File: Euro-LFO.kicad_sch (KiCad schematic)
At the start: 32 parts, among them J1 Conn_02x05_Odd_Even, Q1 NPN, U1 TL074

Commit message: updated
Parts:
- removed Q1: NPN, Package_TO_SOT_SMD:SOT-23, symbol Simulation_SPICE:NPN
- added D4, D5: SS14 (40 V 1 A Schottky), Diode_SMD:D_SMA, symbol Device:D_Schottky
- added J2: Conn_02x10_Odd_Even, symbol Connector_Generic:Conn_02x10_Odd_Even
- added Q1: MMBT3904, Package_TO_SOT_SMD:SOT-23, symbol Transistor_BJT:MMBT3904
- added R23, R24: 10 Ω 0805, Resistor_SMD:R_0805_2012Metric, symbol Device:R_US
- C1, C2: value 47n -> 100 nF 50 V X7R; LCSC (none) -> C49678
- C3: value 47n -> 00 nF 50 V X7R; LCSC (none) -> C49678
- C6, C7: value 47µ -> 10 µF 25 V X5R; footprint (none) -> Capacitor_SMD:C_0805_2012Metric; symbol Device:C_Polarized_Small_US -> Device:C; LCSC (none) -> C15850
- D1, D2: value 1N914 -> 1N4148W; LCSC (none) -> C81598
- D3: value LED -> 3 mm LED
- INV-OUT1, PWM-OUT1, TRI-OUT1: value (none) -> 3.5 mm mono jack, Thonkiconn PJ398SM
- J1: value Conn_02x05_Odd_Even -> 2×5 2.54 mm shrouded IDC box header; footprint Connector_PinHeader_2.54mm:PinHeader_2x05_P2.54mm_Vertical -> Connector_IDC:IDC-Header_2x05_P2.54mm_Vertical
- OFFSET1: value 100K -> 100 kΩ B (linear), centre-detent if available
- R1: value 150K -> 150 kΩ 0805 1%; LCSC (none) -> C17557
- R14, R4: value 4K7 -> 4.7 kΩ 0805 1%; LCSC (none) -> C17673
- R16: value 100K -> 100 kΩ 0805 1%
- R17, R20: value 1K -> 1 kΩ 0805 1%; LCSC (none) -> C17513
- R18, R19, R21, R22, R5: value 100K -> 100 kΩ 0805 1%; LCSC (none) -> C149504
- R2: value 2K2 -> 2.2 kΩ 0805 1%; LCSC (none) -> C17726
- R3: value 1K -> 1 kΩ 0805; LCSC (none) -> C17513
- R6: value 10K -> 10 kΩ 0805 1%; LCSC (none) -> C17414
- RANGE1: value 100K -> 100 kΩ A (audio) for smoother level control (B works)
- RATE1: value 100K -> 100 kΩ Alpha 9 mm vertical - taper B (or reverse‑log for feel)
- SHAPE1: value 500K -> 500 kΩ B (linear)
- U1: value TL074 -> TL074CDR; LCSC (none) -> C6961
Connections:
- net +12V: now also Q1.3 (C), R23.1; no longer J1.1 (Pin_1), J1.2 (Pin_2)
- net -12V: now also R24.1; no longer J1.10 (Pin_10), J1.9 (Pin_9)
- net GND: now also J2.19 (Pin_19)
- net at R14.1: now also Q1.2 (E)
- net LED_A: now reaches D3.2 (A), R14.2
- net LED_A: now also J2.1 (Pin_1)
- net INV-OUT-A: now reaches INV-OUT1.T, R20.1
- net INV-OUT-A: now also J2.3 (Pin_3)
- net at C1.2, R5.1, RANGE1.1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: now also Q1.1 (B)
- net TRI-OUT-A: now reaches R17.1, TRI-OUT1.T
- net TRI-OUT-A: now also J2.5 (Pin_5)
- new net: D5.1 (K), J1.1 (Pin_1), J1.2 (Pin_2)
- new net: D5.2 (A), R24.2
- new net: D4.2 (A), J1.10 (Pin_10), J1.9 (Pin_9)
- new net: D4.1 (K), R23.2
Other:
- moved on the sheet: C2, C3, D2, D3, INV-OUT1, J1, TRI-OUT1, U1E

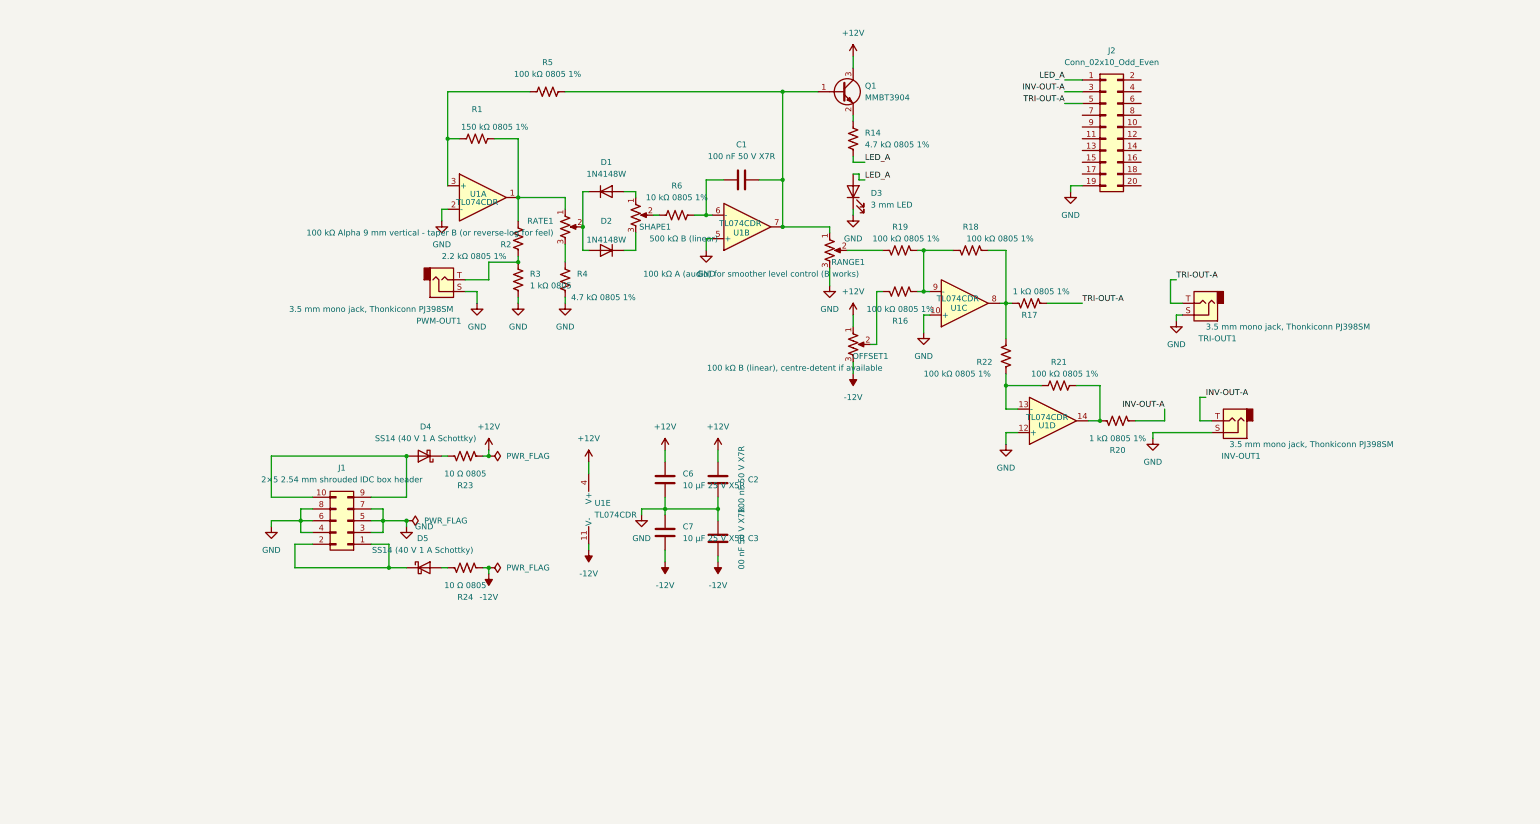
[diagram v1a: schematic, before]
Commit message: added pin headers
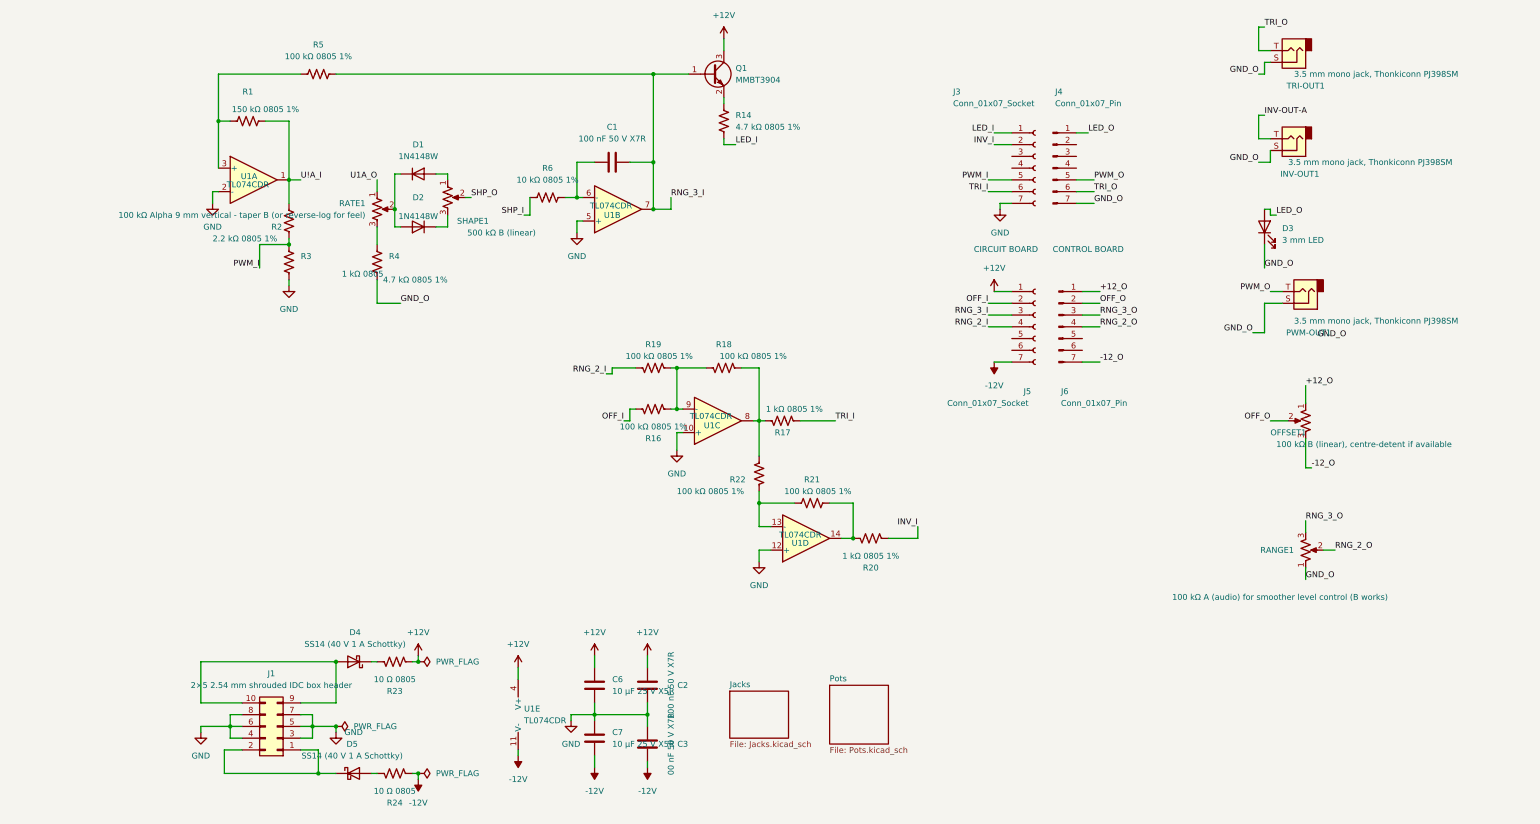
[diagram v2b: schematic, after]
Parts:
- removed J2: Conn_02x10_Odd_Even, symbol Connector_Generic:Conn_02x10_Odd_Even
- added J3, J5: Conn_01x07_Socket, Connector_PinHeader_2.54mm:PinHeader_1x07_P2.54mm_Vertical, symbol Connector:Conn_01x07_Socket
- added J4, J6: Conn_01x07_Pin, Connector_PinHeader_2.54mm:PinHeader_1x07_P2.54mm_Vertical, symbol Connector:Conn_01x07_Pin
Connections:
- net +12V: now also J5.1 (Pin_1); no longer OFFSET1.1
- net -12V: now also J5.7 (Pin_7); no longer OFFSET1.3
- net GND: now also J3.7 (Pin_7); no longer D3.1 (K), INV-OUT1.S, PWM-OUT1.S, R4.1, RANGE1.3, TRI-OUT1.S
- net INV-OUT-A: no longer R20.1
- net U!A_I: now reaches R1.2, R2.2, U1.1
- net U!A_I: no longer RATE1.1
- net PWM_I: now reaches R2.1, R3.2
- net PWM_I: now also J3.5 (Pin_5); no longer PWM-OUT1.T
- net OFF_I: now reaches R16.2
- net OFF_I: now also J5.2 (Pin_2); no longer OFFSET1.2
- net RNG_3_I: now reaches C1.2, Q1.1 (B), R5.1, U1.7
- net RNG_3_I: now also J5.3 (Pin_3); no longer RANGE1.1
- net SHP_I: now reaches R6.2
- net SHP_I: no longer SHAPE1.2
- net RNG_2_I: now reaches R19.2
- net RNG_2_I: now also J5.4 (Pin_4); no longer RANGE1.2
- net LED_A renamed LED_I
- net LED_I: now also J3.1 (Pin_1); no longer D3.2 (A)
- net TRI-OUT-A renamed TRI_I
- net TRI_I: now also J3.6 (Pin_6); no longer TRI-OUT1.T
- new net +12_O: J6.1 (Pin_1), OFFSET1.1
- new net -12_O: J6.7 (Pin_7), OFFSET1.3
- new net GND_O: D3.1 (K), INV-OUT1.S, J4.7 (Pin_7), PWM-OUT1.S, R4.1, RANGE1.1, TRI-OUT1.S
- new net INV_I: J3.2 (Pin_2), R20.1
- new net LED_O: D3.2 (A), J4.1 (Pin_1)
- new net OFF_O: J6.2 (Pin_2), OFFSET1.2
- new net PWM_O: J4.5 (Pin_5), PWM-OUT1.T
- new net RNG_2_O: J6.4 (Pin_4), RANGE1.2
- new net RNG_3_O: J6.3 (Pin_3), RANGE1.3
- new net SHP_O: SHAPE1.2
- new net TRI_O: J4.6 (Pin_6), TRI-OUT1.T
- new net U1A_O: RATE1.1
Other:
- added sheet Jacks (Jacks.kicad_sch)
- added sheet Pots (Pots.kicad_sch)
- note added: "CIRCUIT BOARD"
- note added: "CONTROL BOARD"
- moved on the sheet: C1, C2, C3, C6, C7, D1, D2, D3, D4, D5, INV-OUT1, J1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

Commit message: work in progress
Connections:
- net U!A_I is gone; now on net U1A_I: R1.2, R2.2, U1.1
- net U1A_O: now also J6.5 (Pin_5)
- net U1A_I: now reaches J5.5 (Pin_5)
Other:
- moved on the sheet: C1, D1, D2, Q1, R1, R14, R2, R3, R4, R5, R6, RATE1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

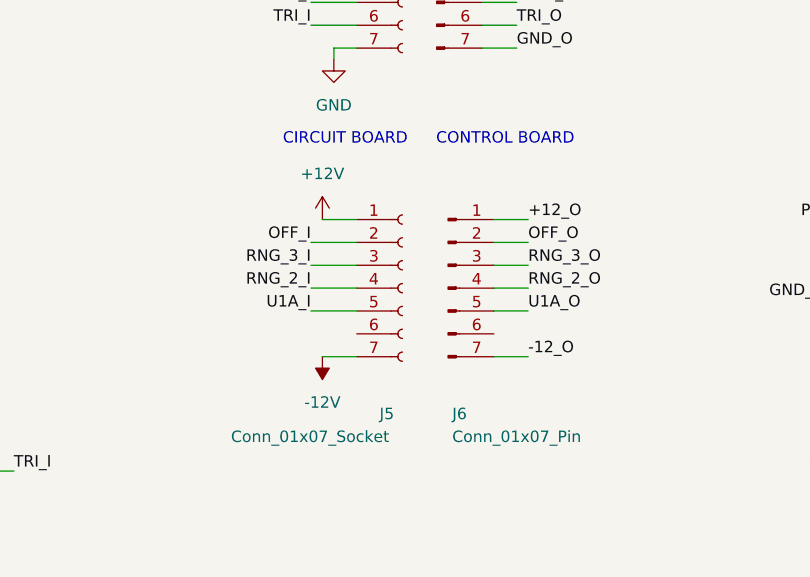
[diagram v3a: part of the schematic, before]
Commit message: Sorting out cross board connections
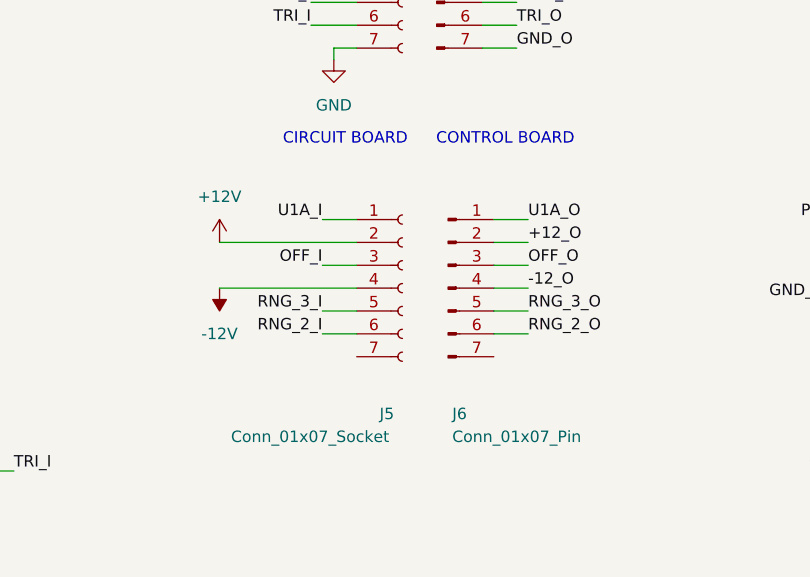
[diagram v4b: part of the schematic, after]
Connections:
- net +12V: now also J5.2 (Pin_2); no longer J5.1 (Pin_1)
- net +12_O: now also J6.2 (Pin_2); no longer J6.1 (Pin_1)
- net -12V: now also J5.4 (Pin_4); no longer J5.7 (Pin_7)
- net -12_O: now also J6.4 (Pin_4); no longer J6.7 (Pin_7)
- net OFF_I: now also J5.3 (Pin_3); no longer J5.2 (Pin_2)
- net OFF_O: now also J6.3 (Pin_3); no longer J6.2 (Pin_2)
- net RNG_2_I: now also J5.6 (Pin_6); no longer J5.4 (Pin_4)
- net RNG_2_O: now also J6.6 (Pin_6); no longer J6.4 (Pin_4)
- net RNG_3_I: now also J5.5 (Pin_5); no longer J5.3 (Pin_3)
- net RNG_3_O: now also J6.5 (Pin_5); no longer J6.3 (Pin_3)
- net U1A_I: now also J5.1 (Pin_1); no longer J5.5 (Pin_5)
- net U1A_O: now also J6.1 (Pin_1); no longer J6.5 (Pin_5)
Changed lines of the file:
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@@
 	(wire
 		(pts
-			(xy 107.95 172.72) (xy 119.38 172.72)
+			(xy 213.36 83.82) (xy 217.17 83.82)
 		)
 		(stroke
@@
 	(wire
 		(pts
-			(xy 132.08 97.79) (xy 125.73 97.79)
+			(xy 107.95 172.72) (xy 119.38 172.72)
 		)
 		(stroke
@@
 	(wire
 		(pts
-			(xy 213.36 86.36) (xy 217.17 86.36)
+			(xy 132.08 97.79) (xy 125.73 97.79)
 		)
 		(stroke
@@
 	(wire
 		(pts
-			(xy 143.51 109.22) (xy 143.51 97.79)
+			(xy 213.36 93.98) (xy 217.17 93.98)
 		)
 		(stroke
@@
 	(wire
 		(pts
-			(xy 52.07 176.53) (xy 52.07 175.26)
+			(xy 143.51 109.22) (xy 143.51 97.79)
 		)
 		(stroke
@@
 	(wire
 		(pts
-			(xy 213.36 91.44) (xy 217.17 91.44)
+			(xy 52.07 176.53) (xy 52.07 175.26)
 		)
 		(stroke
@@
 	(wire
 		(pts
-			(xy 213.36 81.28) (xy 217.17 81.28)
-		)
-		(stroke
-			(width 0)
-			(type default)
-		)
-	)
-	(wire
-		(pts
 			(xy 251.46 48.26) (xy 251.46 43.18)
 		)
@@
 	(wire
 		(pts
+			(xy 194.31 91.44) (xy 198.12 91.44)
+		)
+		(stroke
+			(width 0)
+			(type default)
+		)
+	)
+	(wire
+		(pts
+			(xy 194.31 93.98) (xy 198.12 93.98)
+		)
+		(stroke
+			(width 0)
+			(type default)
+		)
+	)
+	(wire
+		(pts
 			(xy 194.31 46.99) (xy 198.12 46.99)
 		)
@@
 	(wire
 		(pts
-			(xy 193.04 91.44) (xy 198.12 91.44)
-		)
-		(stroke
-			(width 0)
-			(type default)
-		)
-	)
-	(wire
-		(pts
 			(xy 146.05 137.16) (xy 143.51 137.16)
 		)
@@
 	(wire
 		(pts
-			(xy 193.04 86.36) (xy 198.12 86.36)
+			(xy 213.36 86.36) (xy 217.17 86.36)
 		)
 		(stroke
@@
 	(wire
 		(pts
-			(xy 52.07 161.29) (xy 22.86 161.29)
+			(xy 194.31 81.28) (xy 198.12 81.28)
 		)
 		(stroke
@@
 	(wire
 		(pts
-			(xy 251.46 29.21) (xy 251.46 24.13)
+			(xy 52.07 161.29) (xy 22.86 161.29)
 		)
 		(stroke
@@
 	(wire
 		(pts
-			(xy 40.64 54.61) (xy 40.64 44.45)
+			(xy 251.46 29.21) (xy 251.46 24.13)
 		)
 		(stroke
@@
 	(wire
 		(pts
-			(xy 193.04 88.9) (xy 198.12 88.9)
+			(xy 40.64 54.61) (xy 40.64 44.45)
 		)
 		(stroke
@@
 	(wire
 		(pts
-			(xy 213.36 88.9) (xy 217.17 88.9)
-		)
-		(stroke
-			(width 0)
-			(type default)
-		)
-	)
-	(wire
-		(pts
 			(xy 107.95 181.61) (xy 107.95 184.15)
 		)
@@
 	(wire
 		(pts
-			(xy 213.36 96.52) (xy 217.17 96.52)
+			(xy 182.88 88.9) (xy 198.12 88.9)
 		)
 		(stroke
@@
 	(wire
 		(pts
-			(xy 194.31 96.52) (xy 198.12 96.52)
-		)
-		(stroke
-			(width 0)
-			(type default)
-		)
-	)
-	(wire
-		(pts
 			(xy 251.46 53.34) (xy 254 53.34)
 		)
@@
 	(wire
 		(pts
-			(xy 213.36 83.82) (xy 217.17 83.82)
+			(xy 213.36 81.28) (xy 217.17 81.28)
 		)
 		(stroke
@@
 	(wire
 		(pts
+			(xy 213.36 91.44) (xy 217.17 91.44)
+		)
+		(stroke
+			(width 0)
+			(type default)
+		)
+	)
+	(wire
+		(pts
 			(xy 254 50.8) (xy 254 53.34)
 		)
@@
 	(wire
 		(pts
+			(xy 194.31 86.36) (xy 198.12 86.36)
+		)
+		(stroke
+			(width 0)
+			(type default)
+		)
+	)
+	(wire
+		(pts
 			(xy 107.95 170.18) (xy 107.95 172.72)
 		)
@@
 	(wire
 		(pts
-			(xy 143.51 132.08) (xy 146.05 132.08)
+			(xy 213.36 88.9) (xy 217.17 88.9)
 		)
 		(stroke
@@
 	(wire
 		(pts
-			(xy 40.64 44.45) (xy 43.18 44.45)
+			(xy 143.51 132.08) (xy 146.05 132.08)
 		)
 		(stroke
@@
 	(wire
 		(pts
-			(xy 262.89 119.38) (xy 261.62 119.38)
+			(xy 40.64 44.45) (xy 43.18 44.45)
 		)
 		(stroke
@@
 	(wire
 		(pts
-			(xy 152.4 109.22) (xy 160.02 109.22)
+			(xy 262.89 119.38) (xy 261.62 119.38)
 		)
 		(stroke
@@
 	(wire
 		(pts
-			(xy 118.11 66.04) (xy 118.11 68.58)
+			(xy 152.4 109.22) (xy 160.02 109.22)
 		)
 		(stroke
@@
 	(wire
 		(pts
-			(xy 255.27 64.77) (xy 254 64.77)
+			(xy 118.11 66.04) (xy 118.11 68.58)
 		)
 		(stroke
@@
 	(wire
 		(pts
-			(xy 254 64.77) (xy 254 63.5)
+			(xy 255.27 64.77) (xy 254 64.77)
 		)
 		(stroke
@@
 	(wire
 		(pts
-			(xy 171.45 134.62) (xy 177.8 134.62)
+			(xy 254 64.77) (xy 254 63.5)
 		)
 		(stroke
@@
 	(wire
 		(pts
-			(xy 149.86 26.67) (xy 149.86 29.21)
+			(xy 171.45 134.62) (xy 177.8 134.62)
 		)
 		(stroke
@@
 	(wire
 		(pts
-			(xy 22.86 175.26) (xy 29.21 175.26)
+			(xy 182.88 83.82) (xy 198.12 83.82)
 		)
 		(stroke
@@
 	(wire
 		(pts
-			(xy 251.46 24.13) (xy 252.73 24.13)
+			(xy 149.86 26.67) (xy 149.86 29.21)
 		)
 		(stroke
@@
 	(wire
 		(pts
-			(xy 31.75 177.8) (xy 29.21 177.8)
+			(xy 22.86 175.26) (xy 29.21 175.26)
 		)
 		(stroke
@@
 	(wire
 		(pts
-			(xy 29.21 175.26) (xy 29.21 177.8)
+			(xy 251.46 24.13) (xy 252.73 24.13)
 		)
 		(stroke
@@
 	(wire
 		(pts
-			(xy 194.31 81.28) (xy 198.12 81.28)
+			(xy 31.75 177.8) (xy 29.21 177.8)
 		)
 		(stroke
@@
 	(wire
 		(pts
-			(xy 193.04 83.82) (xy 198.12 83.82)
+			(xy 29.21 175.26) (xy 29.21 177.8)
 		)
 		(stroke
@@
 	)
 	(label "+12_O"
-		(at 217.17 81.28 0)
+		(at 217.17 83.82 0)
 		(effects
 			(font
@@
 	)
 	(label "OFF_I"
-		(at 193.04 83.82 180)
+		(at 194.31 86.36 180)
 		(effects
 			(font
@@
 	)
 	(label "RNG_3_I"
-		(at 193.04 86.36 180)
+		(at 194.31 91.44 180)
 		(effects
 			(font
@@
 	)
 	(label "-12_O"
-		(at 217.17 96.52 0)
+		(at 217.17 88.9 0)
 		(effects
 			(font
@@
 	)
 	(label "RNG_2_O"
-		(at 217.17 88.9 0)
+		(at 217.17 93.98 0)
 		(effects
 			(font
@@
 	)
 	(label "RNG_3_O"
-		(at 217.17 86.36 0)
+		(at 217.17 91.44 0)
 		(effects
 			(font
@@
 	)
 	(label "OFF_O"
-		(at 217.17 83.82 0)
+		(at 217.17 86.36 0)
 		(effects
 			(font
@@
 	)
 	(label "U1A_I"
-		(at 193.04 91.44 180)
+		(at 194.31 81.28 180)
 		(effects
 			(font
@@
 	)
 	(label "RNG_2_I"
-		(at 193.04 88.9 180)
+		(at 194.31 93.98 180)
 		(effects
 			(font
@@
 	)
 	(label "U1A_O"
-		(at 217.17 91.44 0)
+		(at 217.17 81.28 0)
 		(effects
 			(font
@@
 	(symbol
 		(lib_id "power:+12V")
-		(at 194.31 81.28 0)
+		(at 182.88 83.82 0)
 		(unit 1)
 		(body_style 1)
@@
 		(fields_autoplaced yes)
 		(property "Reference" "#PWR022"
-			(at 194.31 85.09 0)
+			(at 182.88 87.63 0)
 			(hide yes)
 			(show_name no)
@@
 		)
 		(property "Value" "+12V"
-			(at 194.31 76.2 0)
+			(at 182.88 78.74 0)
 			(show_name no)
 			(do_not_autoplace no)
@@
 		)
 		(property "Footprint" ""
-			(at 194.31 81.28 0)
+			(at 182.88 83.82 0)
 			(hide yes)
 			(show_name no)
@@
 		)
 		(property "Datasheet" ""
-			(at 194.31 81.28 0)
+			(at 182.88 83.82 0)
 			(hide yes)
 			(show_name no)
@@
 		)
 		(property "Description" "Power symbol creates a global label with name \"+12V\""
-			(at 194.31 81.28 0)
+			(at 182.88 83.82 0)
 			(hide yes)
 			(show_name no)
@@
 	(symbol
 		(lib_id "power:-12V")
-		(at 194.31 96.52 180)
+		(at 182.88 88.9 180)
 		(unit 1)
 		(body_style 1)
@@
 		(fields_autoplaced yes)
 		(property "Reference" "#PWR031"
-			(at 194.31 92.71 0)
+			(at 182.88 85.09 0)
 			(hide yes)
 			(show_name no)
@@
 		)
 		(property "Value" "-12V"
-			(at 194.31 101.6 0)
+			(at 182.88 93.98 0)
 			(show_name no)
 			(do_not_autoplace no)
@@
 		)
 		(property "Footprint" ""
-			(at 194.31 96.52 0)
+			(at 182.88 88.9 0)
 			(hide yes)
 			(show_name no)
@@
 		)
 		(property "Datasheet" ""
-			(at 194.31 96.52 0)
+			(at 182.88 88.9 0)
 			(hide yes)
 			(show_name no)
@@
 		)
 		(property "Description" "Power symbol creates a global label with name \"-12V\""
-			(at 194.31 96.52 0)
+			(at 182.88 88.9 0)
 			(hide yes)
 			(show_name no)
